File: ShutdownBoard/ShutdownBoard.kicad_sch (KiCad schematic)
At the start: 2 parts

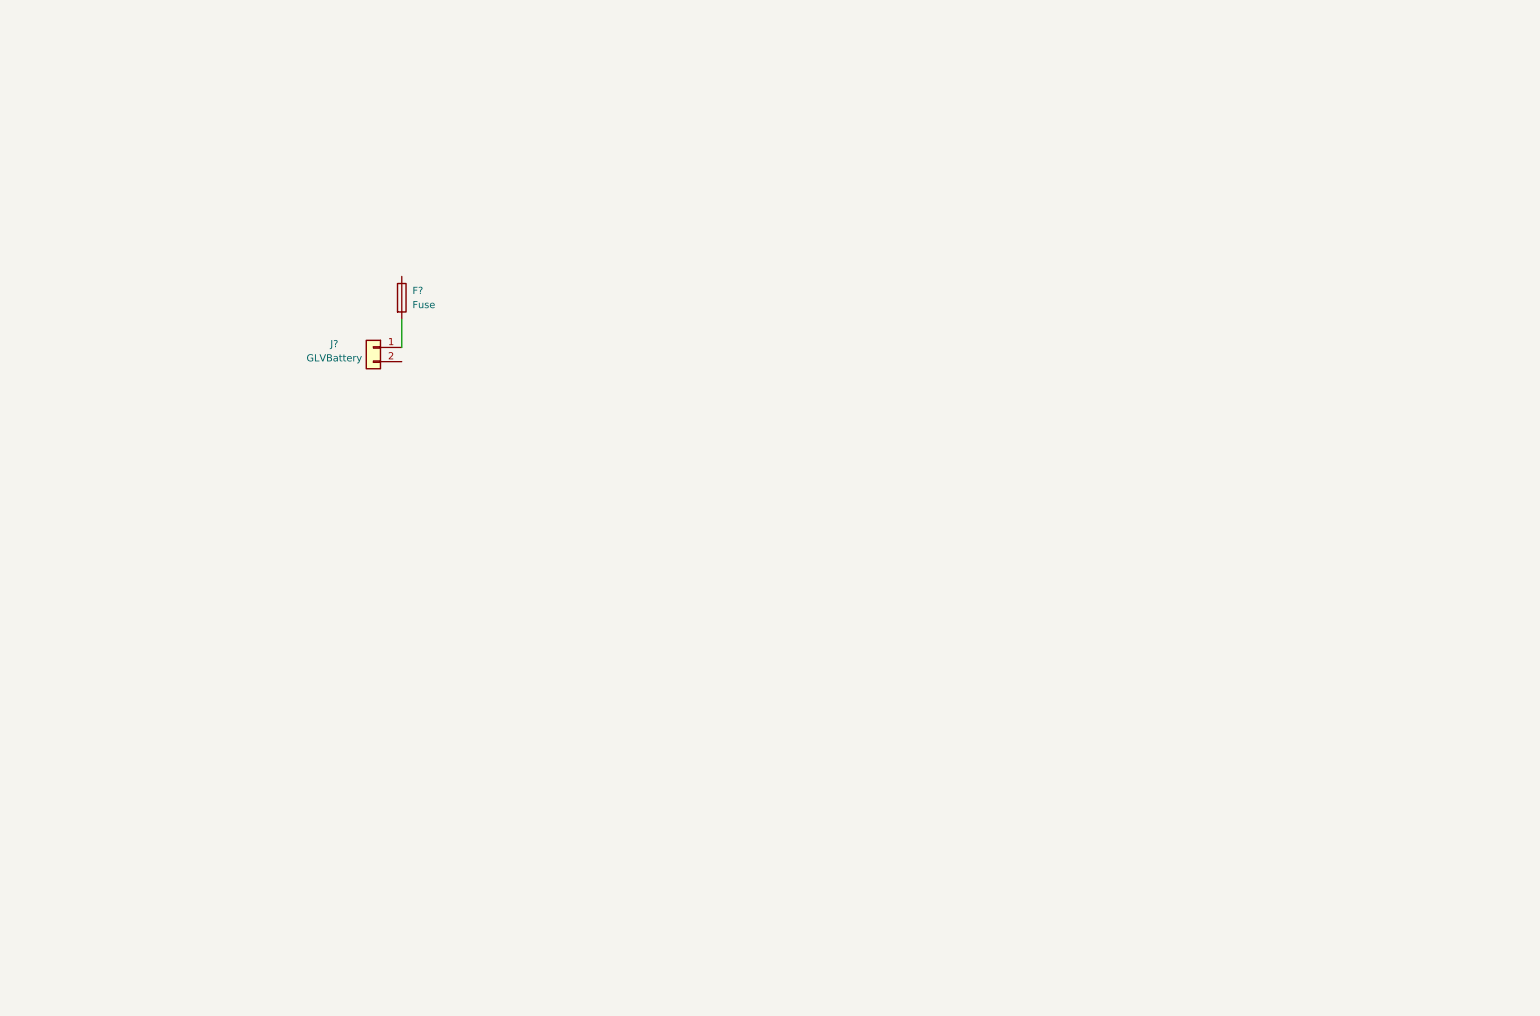
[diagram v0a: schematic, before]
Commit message: Update ShutdownBoard.kicad_sch
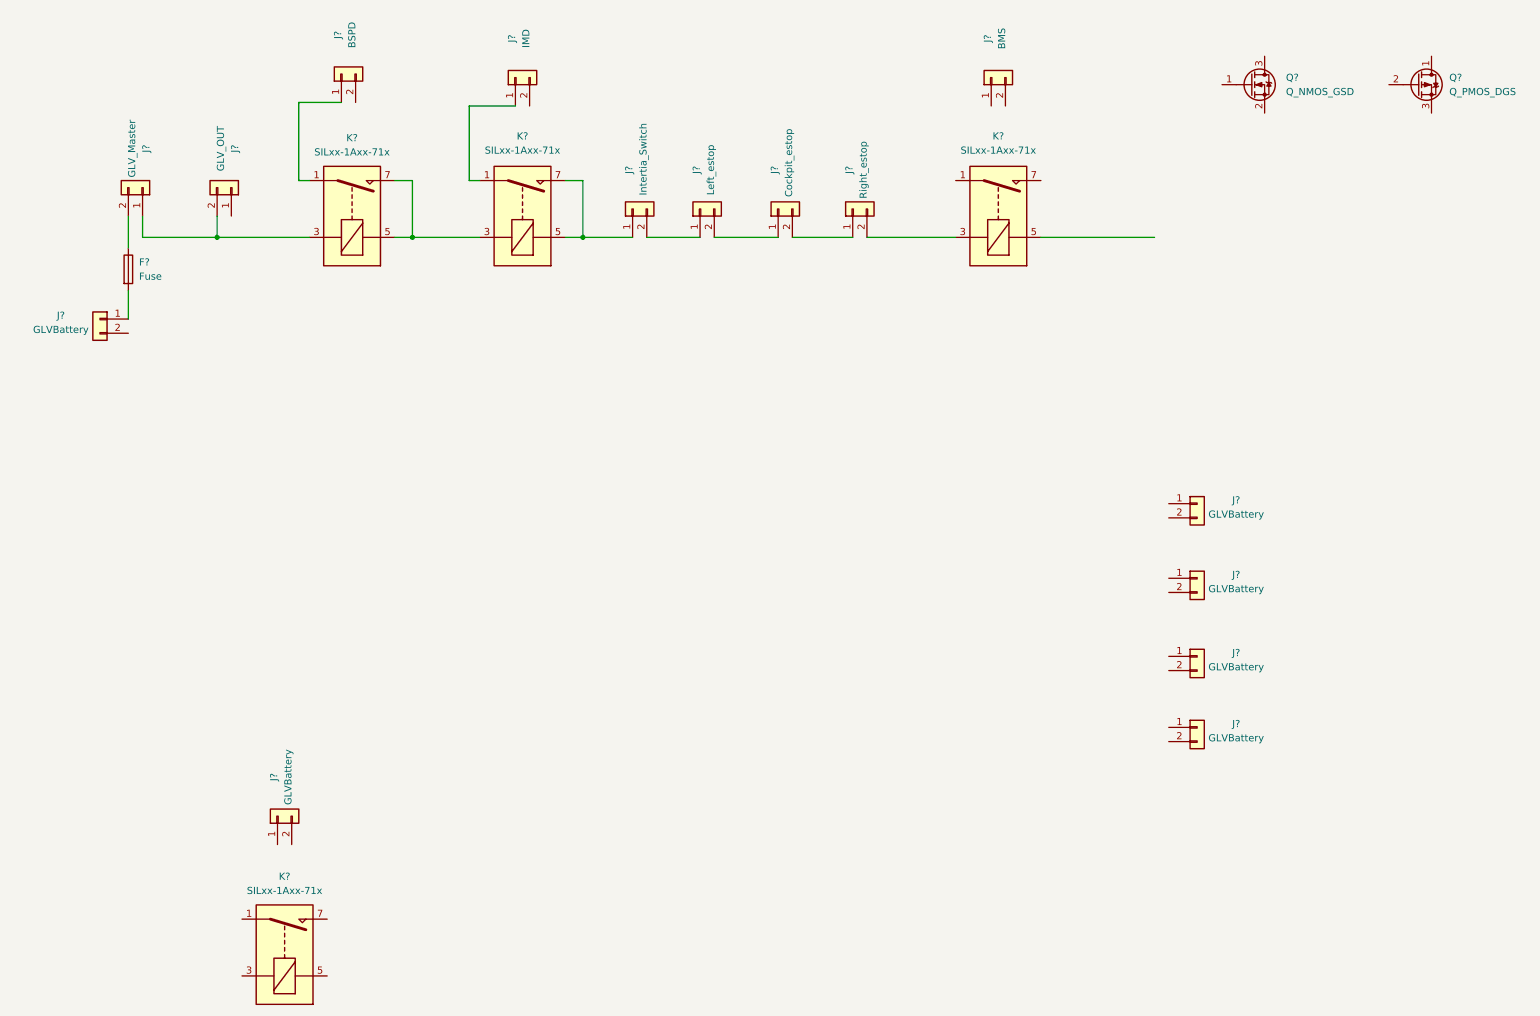
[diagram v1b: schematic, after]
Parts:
- added J? (x5): GLVBattery, symbol GRC_Connector:Conn_01x02
- added J?: GLV_Master, symbol GRC_Connector:Conn_01x02
- added J?: IMD, symbol GRC_Connector:Conn_01x02
- added J?: BMS, symbol GRC_Connector:Conn_01x02
- added J?: BSPD, symbol GRC_Connector:Conn_01x02
- added J?: GLV_OUT, symbol GRC_Connector:Conn_01x02
- added J?: Intertia_Switch, symbol GRC_Connector:Conn_01x02
- added J?: Right_estop, symbol GRC_Connector:Conn_01x02
- added J?: Cockpit_estop, symbol GRC_Connector:Conn_01x02
- added J?: Left_estop, symbol GRC_Connector:Conn_01x02
- added K? (x4): SILxx-1Axx-71x, Relay_THT:Relay_SPST_StandexMeder_SIL_Form1A, symbol GRC_Relay:SILxx-1Axx-71x
- added Q?: Q_NMOS_GSD, symbol GRC_Device:Q_NMOS_GSD
- added Q?: Q_PMOS_DGS, symbol GRC_Device:Q_PMOS_DGS
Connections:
- net at F?.1: now also J?.2 (Pin_2)
- new net: J?.2 (Pin_2), K?.3
- new net: J?.1 (Pin_1), J?.2 (Pin_2), K?.3
- new net: J?.1 (Pin_1), K?.1 (x2)
- new net: K?.3, K?.5, K?.7
- new net: J?.1 (Pin_1), K?.5, K?.7
- new net: J?.1 (Pin_1), J?.2 (Pin_2) (x3)
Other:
- moved on the sheet: F?, J?

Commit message: Update ShutdownBoard.kicad_sch
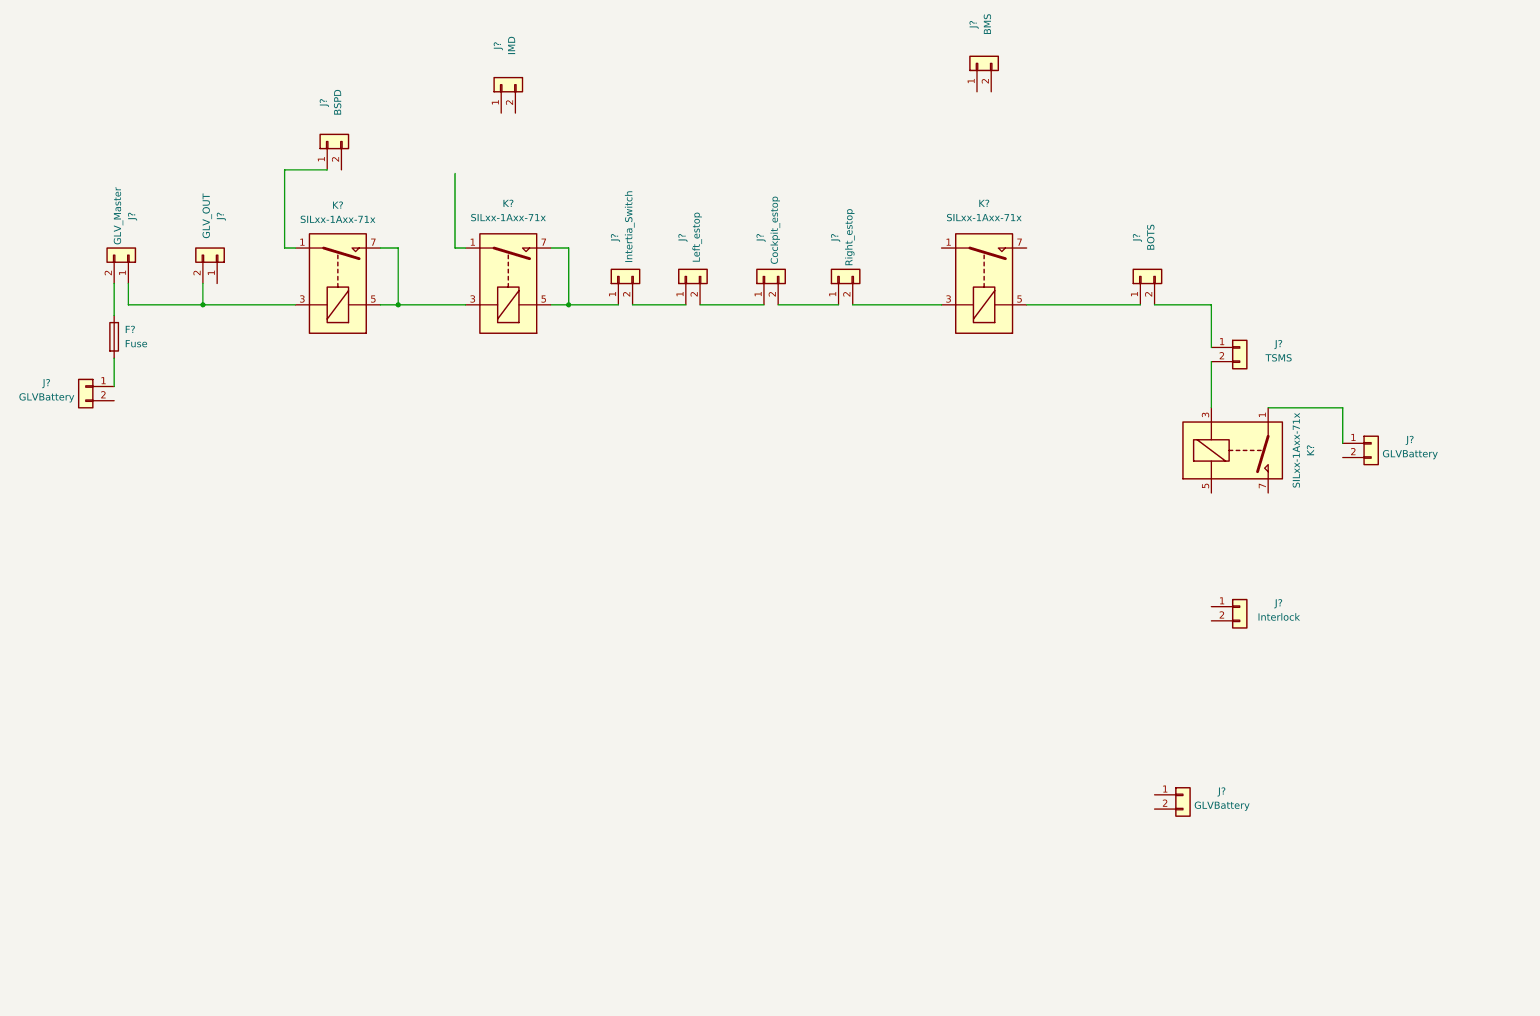
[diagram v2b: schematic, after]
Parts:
- removed Q?: Q_NMOS_GSD, symbol GRC_Device:Q_NMOS_GSD
- removed Q?: Q_PMOS_DGS, symbol GRC_Device:Q_PMOS_DGS
- J?: value GLVBattery -> BOTS
- J?: value GLVBattery -> Interlock
- J?: value GLVBattery -> TSMS
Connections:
- net at K?.1: now also J?.1 (Pin_1)
- net at K?.3: now also J?.2 (Pin_2)
- net at K?.5: now also J?.1 (Pin_1)
- net at J?.2 (Pin_2): now also J?.1 (Pin_1)
- net at J?.1 (Pin_1): no longer K?.1
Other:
- moved on the sheet: F?, J?, K?

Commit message: Update ShutdownBoard.kicad_sch
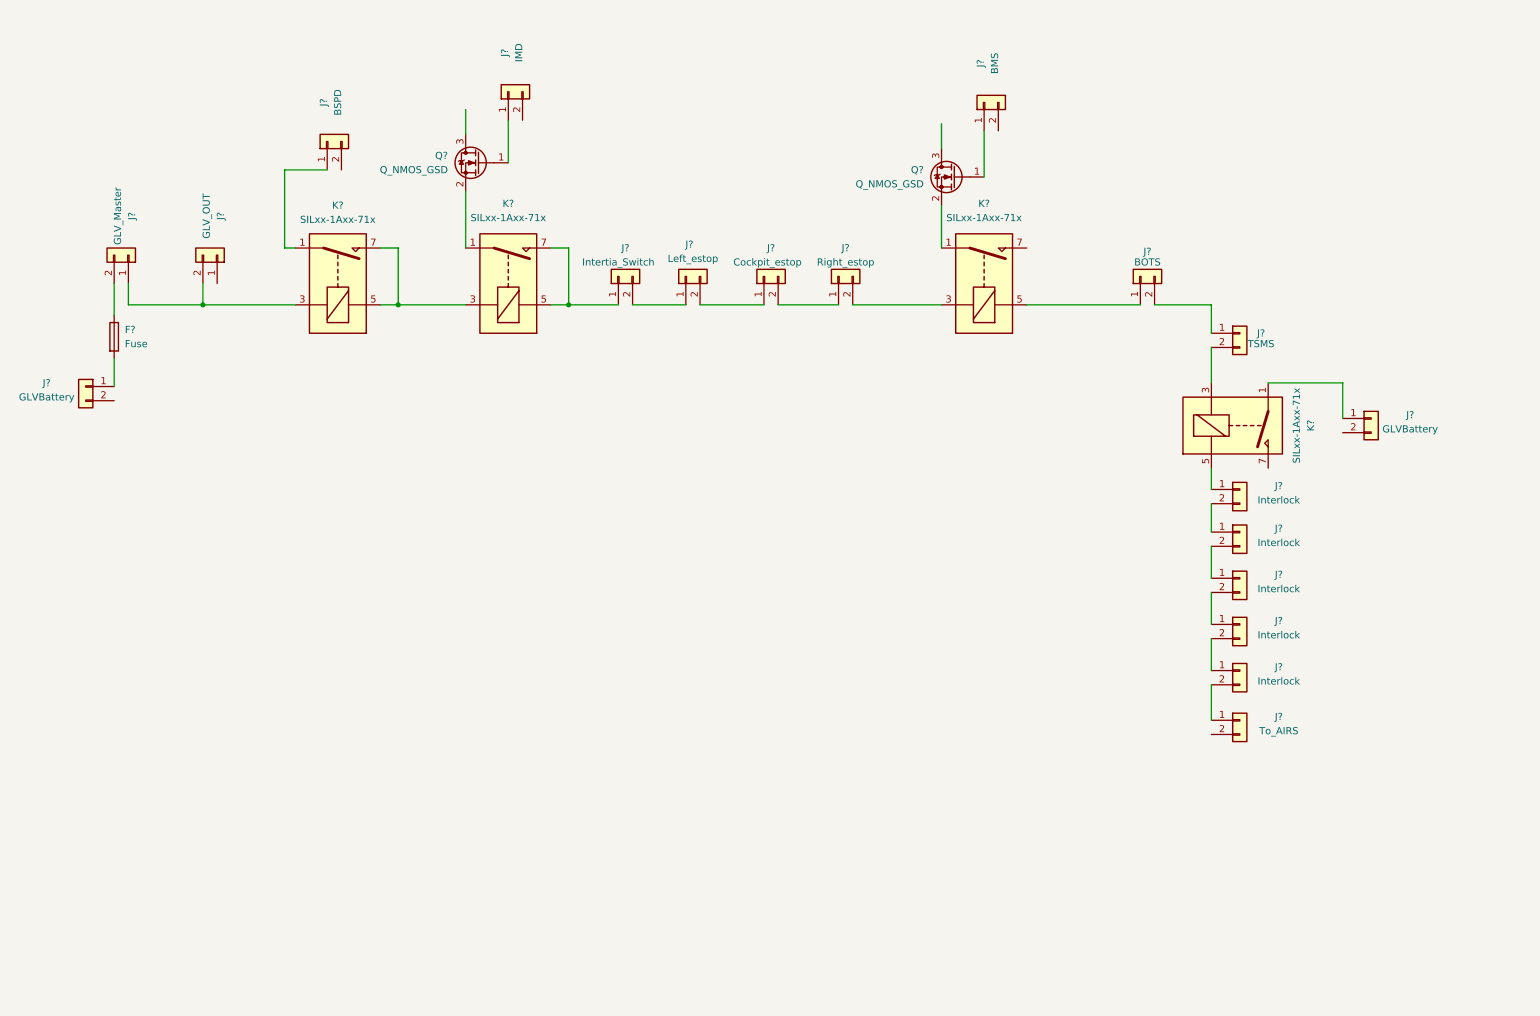
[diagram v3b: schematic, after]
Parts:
- added J? (x4): Interlock, symbol GRC_Connector:Conn_01x02
- added Q? (x2): Q_NMOS_GSD, symbol GRC_Device:Q_NMOS_GSD
- J?: value GLVBattery -> To_AIRS
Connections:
- net at K?.5: now also J?.1 (Pin_1)
- net at K?.1: now also Q?.2 (S) (x2)
- net at J?.2 (Pin_2): now also J?.1 (Pin_1)
- net at J?.1 (Pin_1): now also J?.2 (Pin_2)
- net at J?.1 (Pin_1): now also Q?.1 (G) (x2)
- new net: J?.1 (Pin_1), J?.2 (Pin_2) (x3)
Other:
- moved on the sheet: J?, K?
